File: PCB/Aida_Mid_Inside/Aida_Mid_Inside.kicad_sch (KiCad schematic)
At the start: 14 parts

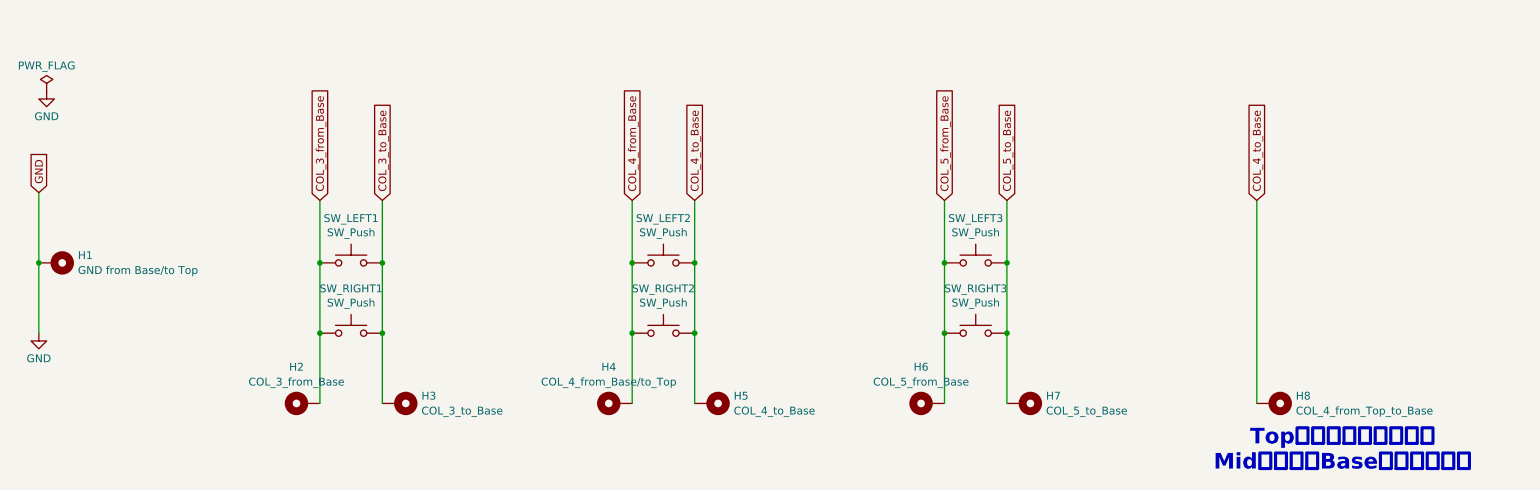
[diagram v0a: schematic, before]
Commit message: テストポイントを追加、配置した。
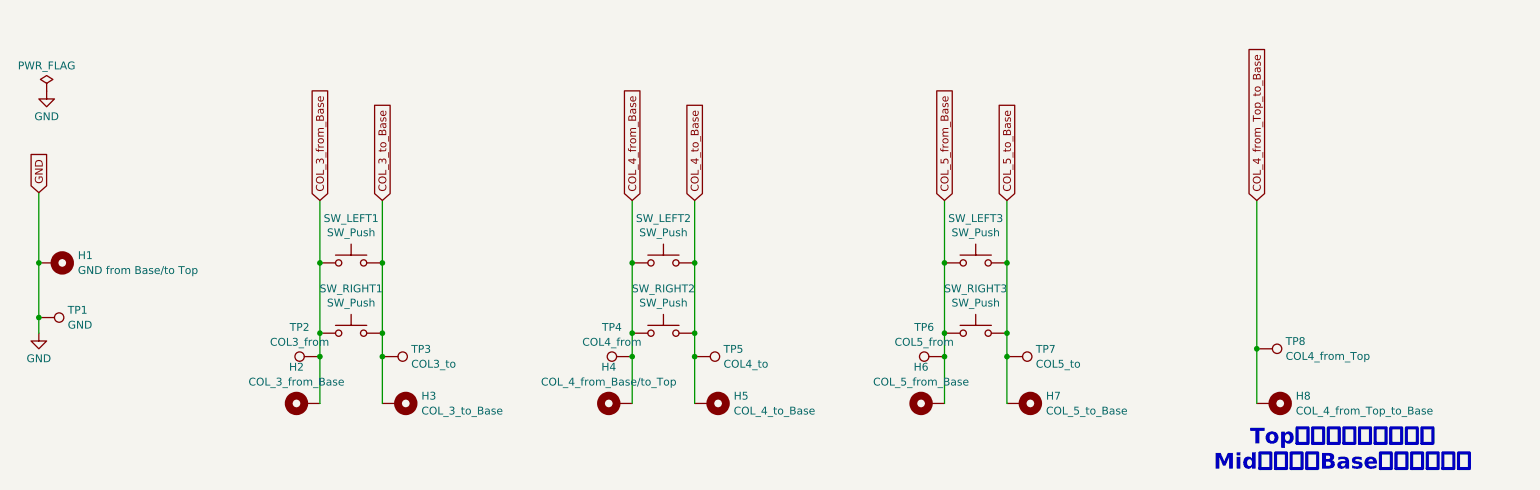
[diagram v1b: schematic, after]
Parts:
- added TP1: GND, Connector_PinHeader_2.00mm:PinHeader_1x01_P2.00mm_Vertical, symbol Connector:TestPoint
- added TP2: COL3_from, Connector_PinHeader_2.00mm:PinHeader_1x01_P2.00mm_Vertical, symbol Connector:TestPoint
- added TP3: COL3_to, Connector_PinHeader_2.00mm:PinHeader_1x01_P2.00mm_Vertical, symbol Connector:TestPoint
- added TP4: COL4_from, Connector_PinHeader_2.00mm:PinHeader_1x01_P2.00mm_Vertical, symbol Connector:TestPoint
- added TP5: COL4_to, Connector_PinHeader_2.00mm:PinHeader_1x01_P2.00mm_Vertical, symbol Connector:TestPoint
- added TP6: COL5_from, Connector_PinHeader_2.00mm:PinHeader_1x01_P2.00mm_Vertical, symbol Connector:TestPoint
- added TP7: COL5_to, Connector_PinHeader_2.00mm:PinHeader_1x01_P2.00mm_Vertical, symbol Connector:TestPoint
- added TP8: COL4_from_Top, Connector_PinHeader_2.00mm:PinHeader_1x01_P2.00mm_Vertical, symbol Connector:TestPoint
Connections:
- net COL_3_from_Base: now also TP2.1
- net COL_3_to_Base: now also TP3.1
- net COL_4_from_Base: now also TP4.1
- net COL_4_to_Base: now also TP5.1; no longer H8.1
- net COL_5_from_Base: now also TP6.1
- net COL_5_to_Base: now also TP7.1
- net GND: now also TP1.1
- new net COL_4_from_Top_to_Base: H8.1, TP8.1
